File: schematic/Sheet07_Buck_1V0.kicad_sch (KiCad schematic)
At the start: 14 parts, among them U5 TPS7H5001-SP

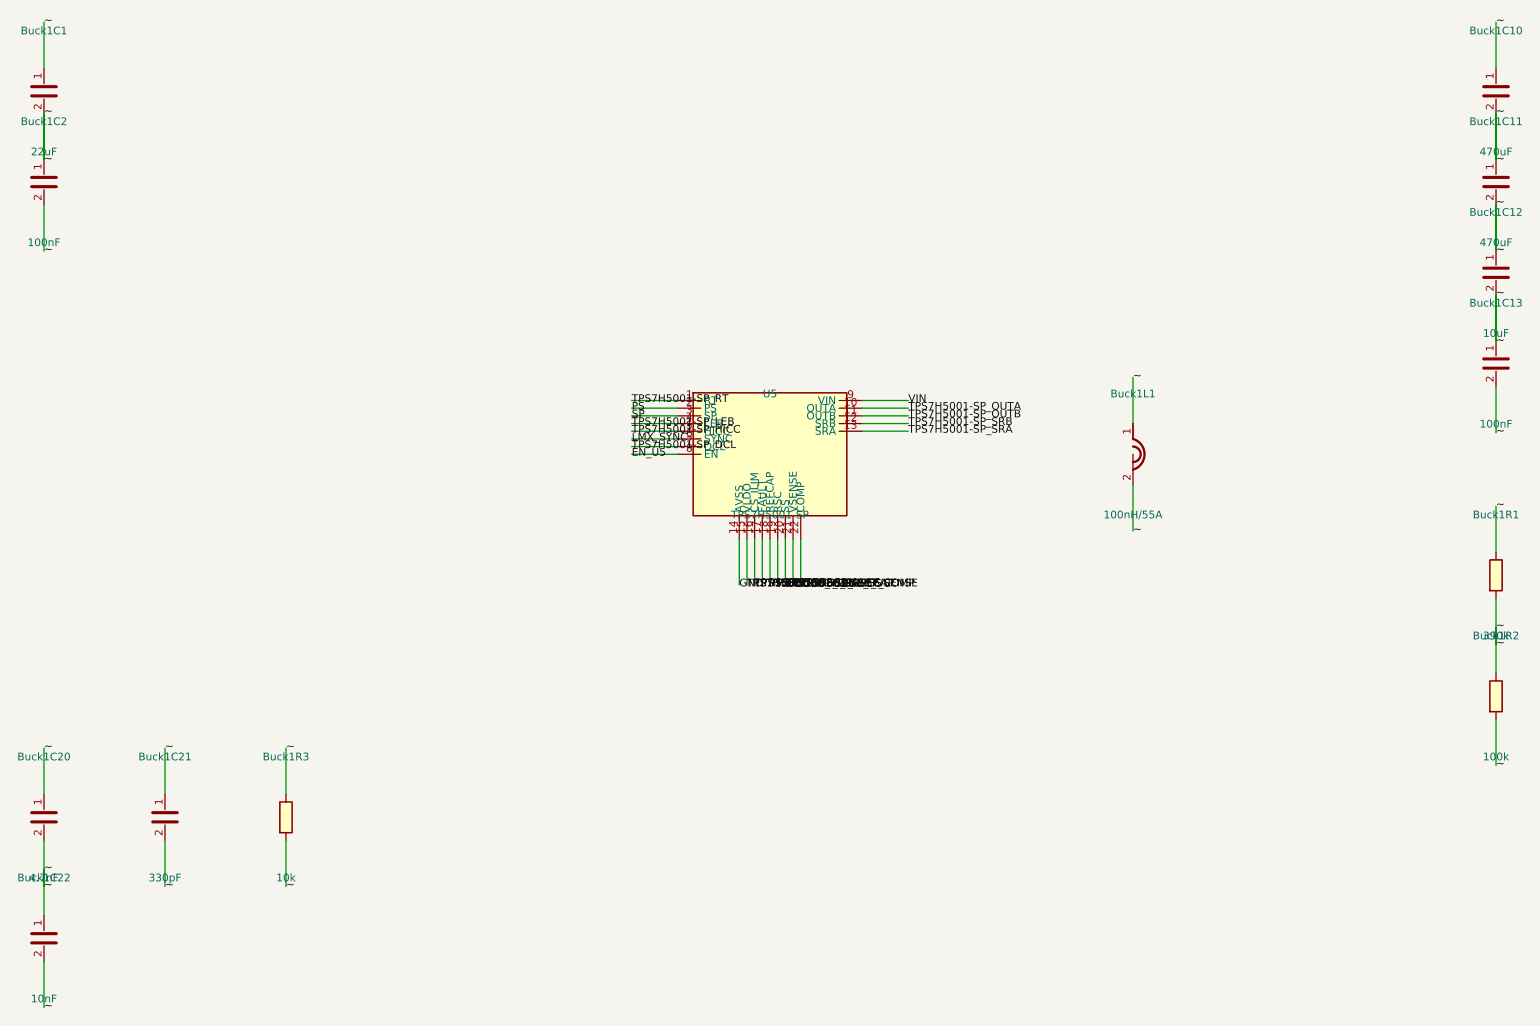
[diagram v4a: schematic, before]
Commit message: fix: use horizontal wire stubs to prevent KiCad net merging
Root cause: vertical wires from stacked power pins (1.27mm spacing)
overlapped when wire length > pin spacing, causing KiCad to merge
all power nets into one. Also skip unnamed (~) passive component pins.

Changes:
- Always use horizontal LEFT stubs regardless of pin angle
- Skip pins with net_name '~' (capacitor/resistor unnamed pins)
- 557 pin connections across 13 sheets, all pass KiCad CLI

NOTE: power net separation still shows all power_in pins on one net
in kicad-cli netlist export - needs further investigation.
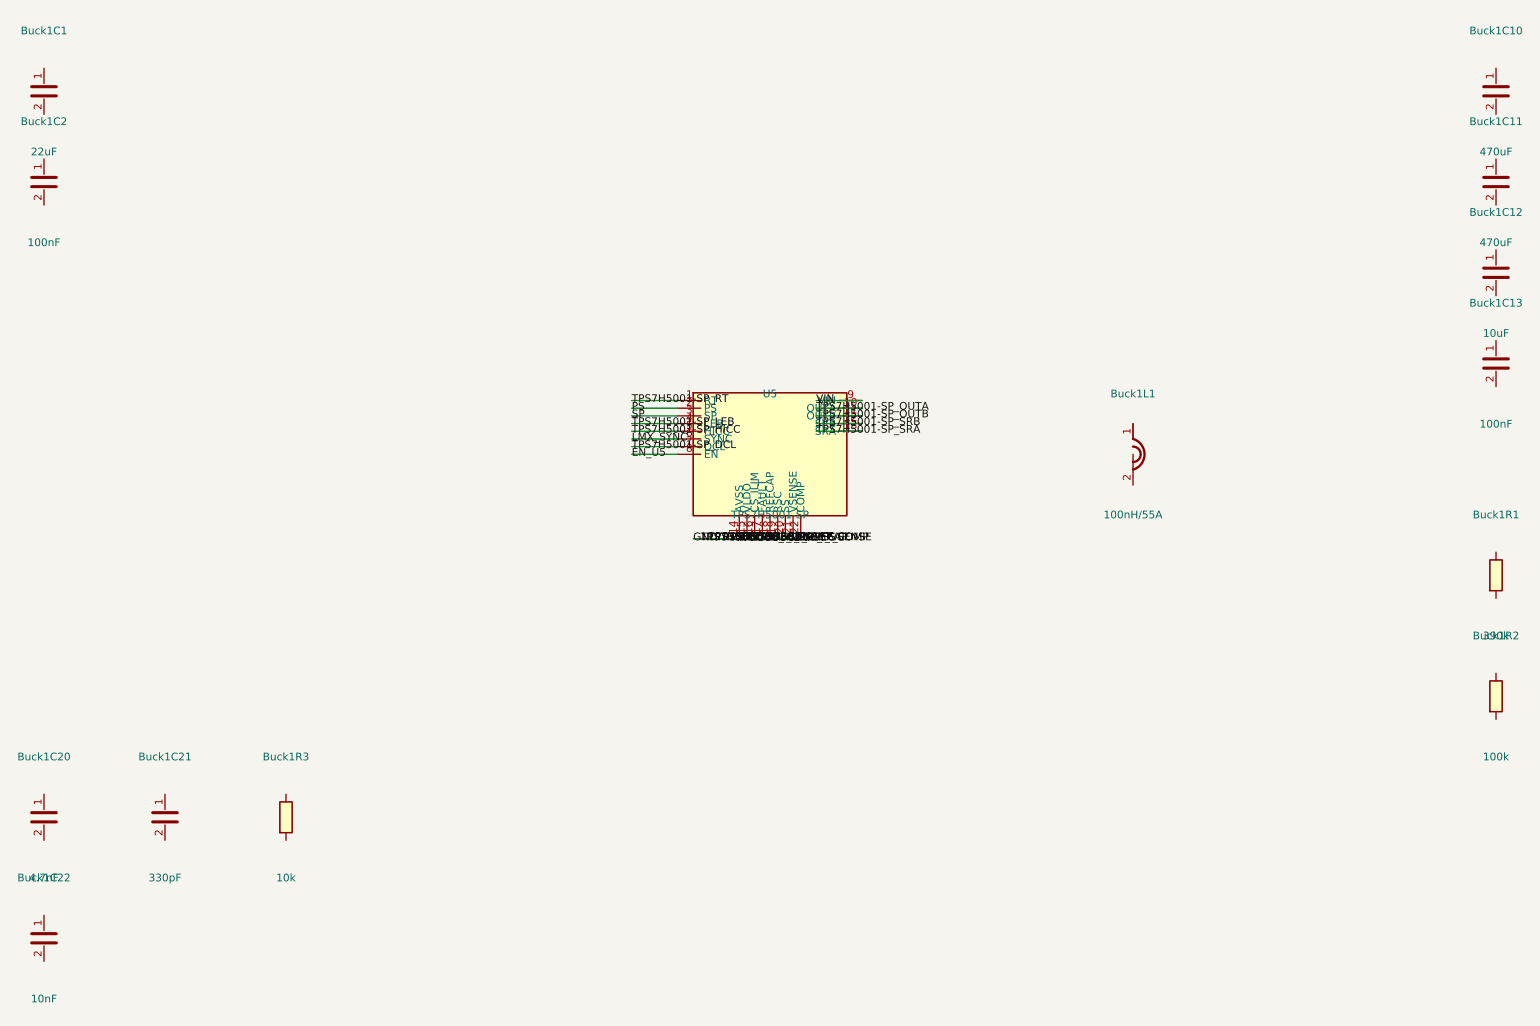
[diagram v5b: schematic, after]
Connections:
- net RSC is gone; now on net GND: U5.19 (RSC)
- net TPS7H5001-SP_COMP is gone; now on net GND: U5.22 (COMP)
- net TPS7H5001-SP_CS is gone; now on net GND: U5.16 (CS_ILIM)
- net TPS7H5001-SP_FAULT is gone; now on net GND: U5.17 (FAULT)
- net TPS7H5001-SP_REFCAP is gone; now on net GND: U5.18 (REFCAP)
- net TPS7H5001-SP_SS is gone; now on net GND: U5.20 (SS)
- net TPS7H5001-SP_VLDO is gone; now on net GND: U5.15 (VLDO)
- net TPS7H5001-SP_VSENSE is gone; now on net GND: U5.21 (VSENSE)
- removed net ~: Buck1C1.1, Buck1C1.2, Buck1C10.1, Buck1C10.2, Buck1C11.1, Buck1C11.2, Buck1C12.1, Buck1C12.2, Buck1C13.1, Buck1C13.2, Buck1C2.1, Buck1C2.2, Buck1C20.1, Buck1C20.2, Buck1C21.1, Buck1C21.2, Buck1C22.1, Buck1C22.2, Buck1L1.1, Buck1L1.2, Buck1R1.1, Buck1R1.2, Buck1R2.1, Buck1R2.2, Buck1R3.1, Buck1R3.2
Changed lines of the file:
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@@
   (wire (pts (xy 184.7600 100.0000) (xy 177.1400 100.0000)) (stroke (width 0) (type default)))
   (label "EN_U5" (at 177.1400 100.0000 0) (effects (font (size 1.27 1.27))))
-  (wire (pts (xy 215.2400 91.1100) (xy 222.8600 91.1100)) (stroke (width 0) (type default)))
-  (label "VIN" (at 222.8600 91.1100 0) (effects (font (size 1.27 1.27))))
-  (wire (pts (xy 215.2400 92.3800) (xy 222.8600 92.3800)) (stroke (width 0) (type default)))
-  (label "TPS7H5001-SP_OUTA" (at 222.8600 92.3800 0) (effects (font (size 1.27 1.27))))
-  (wire (pts (xy 215.2400 93.6500) (xy 222.8600 93.6500)) (stroke (width 0) (type default)))
-  (label "TPS7H5001-SP_OUTB" (at 222.8600 93.6500 0) (effects (font (size 1.27 1.27))))
-  (wire (pts (xy 215.2400 94.9200) (xy 222.8600 94.9200)) (stroke (width 0) (type default)))
-  (label "TPS7H5001-SP_SRB" (at 222.8600 94.9200 0) (effects (font (size 1.27 1.27))))
-  (wire (pts (xy 215.2400 96.1900) (xy 222.8600 96.1900)) (stroke (width 0) (type default)))
-  (label "TPS7H5001-SP_SRA" (at 222.8600 96.1900 0) (effects (font (size 1.27 1.27))))
-  (wire (pts (xy 194.9200 113.9700) (xy 194.9200 121.5900)) (stroke (width 0) (type default)))
-  (label "GND" (at 194.9200 121.5900 0) (effects (font (size 1.27 1.27))))
-  (wire (pts (xy 196.1900 113.9700) (xy 196.1900 121.5900)) (stroke (width 0) (type default)))
-  (label "TPS7H5001-SP_VLDO" (at 196.1900 121.5900 0) (effects (font (size 1.27 1.27))))
-  (wire (pts (xy 197.4600 113.9700) (xy 197.4600 121.5900)) (stroke (width 0) (type default)))
-  (label "TPS7H5001-SP_CS" (at 197.4600 121.5900 0) (effects (font (size 1.27 1.27))))
-  (wire (pts (xy 198.7300 113.9700) (xy 198.7300 121.5900)) (stroke (width 0) (type default)))
-  (label "TPS7H5001-SP_FAULT" (at 198.7300 121.5900 0) (effects (font (size 1.27 1.27))))
-  (wire (pts (xy 200.0000 113.9700) (xy 200.0000 121.5900)) (stroke (width 0) (type default)))
-  (label "TPS7H5001-SP_REFCAP" (at 200.0000 121.5900 0) (effects (font (size 1.27 1.27))))
-  (wire (pts (xy 201.2700 113.9700) (xy 201.2700 121.5900)) (stroke (width 0) (type default)))
-  (label "RSC" (at 201.2700 121.5900 0) (effects (font (size 1.27 1.27))))
-  (wire (pts (xy 202.5400 113.9700) (xy 202.5400 121.5900)) (stroke (width 0) (type default)))
-  (label "TPS7H5001-SP_SS" (at 202.5400 121.5900 0) (effects (font (size 1.27 1.27))))
-  (wire (pts (xy 203.8100 113.9700) (xy 203.8100 121.5900)) (stroke (width 0) (type default)))
-  (label "TPS7H5001-SP_VSENSE" (at 203.8100 121.5900 0) (effects (font (size 1.27 1.27))))
-  (wire (pts (xy 205.0800 113.9700) (xy 205.0800 121.5900)) (stroke (width 0) (type default)))
-  (label "TPS7H5001-SP_COMP" (at 205.0800 121.5900 0) (effects (font (size 1.27 1.27))))
-  (wire (pts (xy 80.0000 36.1900) (xy 80.0000 28.5700)) (stroke (width 0) (type default)))
-  (label "~" (at 80.0000 28.5700 0) (effects (font (size 1.27 1.27))))
-  (wire (pts (xy 80.0000 43.8100) (xy 80.0000 51.4300)) (stroke (width 0) (type default)))
-  (label "~" (at 80.0000 51.4300 0) (effects (font (size 1.27 1.27))))
-  (wire (pts (xy 80.0000 51.1900) (xy 80.0000 43.5700)) (stroke (width 0) (type default)))
-  (label "~" (at 80.0000 43.5700 0) (effects (font (size 1.27 1.27))))
-  (wire (pts (xy 80.0000 58.8100) (xy 80.0000 66.4300)) (stroke (width 0) (type default)))
-  (label "~" (at 80.0000 66.4300 0) (effects (font (size 1.27 1.27))))
-  (wire (pts (xy 320.0000 36.1900) (xy 320.0000 28.5700)) (stroke (width 0) (type default)))
-  (label "~" (at 320.0000 28.5700 0) (effects (font (size 1.27 1.27))))
-  (wire (pts (xy 320.0000 43.8100) (xy 320.0000 51.4300)) (stroke (width 0) (type default)))
-  (label "~" (at 320.0000 51.4300 0) (effects (font (size 1.27 1.27))))
-  (wire (pts (xy 320.0000 51.1900) (xy 320.0000 43.5700)) (stroke (width 0) (type default)))
-  (label "~" (at 320.0000 43.5700 0) (effects (font (size 1.27 1.27))))
-  (wire (pts (xy 320.0000 58.8100) (xy 320.0000 66.4300)) (stroke (width 0) (type default)))
-  (label "~" (at 320.0000 66.4300 0) (effects (font (size 1.27 1.27))))
-  (wire (pts (xy 320.0000 66.1900) (xy 320.0000 58.5700)) (stroke (width 0) (type default)))
-  (label "~" (at 320.0000 58.5700 0) (effects (font (size 1.27 1.27))))
-  (wire (pts (xy 320.0000 73.8100) (xy 320.0000 81.4300)) (stroke (width 0) (type default)))
-  (label "~" (at 320.0000 81.4300 0) (effects (font (size 1.27 1.27))))
-  (wire (pts (xy 320.0000 81.1900) (xy 320.0000 73.5700)) (stroke (width 0) (type default)))
-  (label "~" (at 320.0000 73.5700 0) (effects (font (size 1.27 1.27))))
-  (wire (pts (xy 320.0000 88.8100) (xy 320.0000 96.4300)) (stroke (width 0) (type default)))
-  (label "~" (at 320.0000 96.4300 0) (effects (font (size 1.27 1.27))))
-  (wire (pts (xy 260.0000 94.9200) (xy 260.0000 87.3000)) (stroke (width 0) (type default)))
-  (label "~" (at 260.0000 87.3000 0) (effects (font (size 1.27 1.27))))
-  (wire (pts (xy 260.0000 105.0800) (xy 260.0000 112.7000)) (stroke (width 0) (type default)))
-  (label "~" (at 260.0000 112.7000 0) (effects (font (size 1.27 1.27))))
-  (wire (pts (xy 320.0000 116.1900) (xy 320.0000 108.5700)) (stroke (width 0) (type default)))
-  (label "~" (at 320.0000 108.5700 0) (effects (font (size 1.27 1.27))))
-  (wire (pts (xy 320.0000 123.8100) (xy 320.0000 131.4300)) (stroke (width 0) (type default)))
-  (label "~" (at 320.0000 131.4300 0) (effects (font (size 1.27 1.27))))
-  (wire (pts (xy 320.0000 136.1900) (xy 320.0000 128.5700)) (stroke (width 0) (type default)))
-  (label "~" (at 320.0000 128.5700 0) (effects (font (size 1.27 1.27))))
-  (wire (pts (xy 320.0000 143.8100) (xy 320.0000 151.4300)) (stroke (width 0) (type default)))
-  (label "~" (at 320.0000 151.4300 0) (effects (font (size 1.27 1.27))))
-  (wire (pts (xy 80.0000 156.1900) (xy 80.0000 148.5700)) (stroke (width 0) (type default)))
-  (label "~" (at 80.0000 148.5700 0) (effects (font (size 1.27 1.27))))
-  (wire (pts (xy 80.0000 163.8100) (xy 80.0000 171.4300)) (stroke (width 0) (type default)))
-  (label "~" (at 80.0000 171.4300 0) (effects (font (size 1.27 1.27))))
-  (wire (pts (xy 100.0000 156.1900) (xy 100.0000 148.5700)) (stroke (width 0) (type default)))
-  (label "~" (at 100.0000 148.5700 0) (effects (font (size 1.27 1.27))))
-  (wire (pts (xy 100.0000 163.8100) (xy 100.0000 171.4300)) (stroke (width 0) (type default)))
-  (label "~" (at 100.0000 171.4300 0) (effects (font (size 1.27 1.27))))
-  (wire (pts (xy 120.0000 156.1900) (xy 120.0000 148.5700)) (stroke (width 0) (type default)))
-  (label "~" (at 120.0000 148.5700 0) (effects (font (size 1.27 1.27))))
-  (wire (pts (xy 120.0000 163.8100) (xy 120.0000 171.4300)) (stroke (width 0) (type default)))
-  (label "~" (at 120.0000 171.4300 0) (effects (font (size 1.27 1.27))))
-  (wire (pts (xy 80.0000 176.1900) (xy 80.0000 168.5700)) (stroke (width 0) (type default)))
-  (label "~" (at 80.0000 168.5700 0) (effects (font (size 1.27 1.27))))
-  (wire (pts (xy 80.0000 183.8100) (xy 80.0000 191.4300)) (stroke (width 0) (type default)))
-  (label "~" (at 80.0000 191.4300 0) (effects (font (size 1.27 1.27))))
+  (wire (pts (xy 215.2400 91.1100) (xy 207.6200 91.1100)) (stroke (width 0) (type default)))
+  (label "VIN" (at 207.6200 91.1100 0) (effects (font (size 1.27 1.27))))
+  (wire (pts (xy 215.2400 92.3800) (xy 207.6200 92.3800)) (stroke (width 0) (type default)))
+  (label "TPS7H5001-SP_OUTA" (at 207.6200 92.3800 0) (effects (font (size 1.27 1.27))))
+  (wire (pts (xy 215.2400 93.6500) (xy 207.6200 93.6500)) (stroke (width 0) (type default)))
+  (label "TPS7H5001-SP_OUTB" (at 207.6200 93.6500 0) (effects (font (size 1.27 1.27))))
+  (wire (pts (xy 215.2400 94.9200) (xy 207.6200 94.9200)) (stroke (width 0) (type default)))
+  (label "TPS7H5001-SP_SRB" (at 207.6200 94.9200 0) (effects (font (size 1.27 1.27))))
+  (wire (pts (xy 215.2400 96.1900) (xy 207.6200 96.1900)) (stroke (width 0) (type default)))
+  (label "TPS7H5001-SP_SRA" (at 207.6200 96.1900 0) (effects (font (size 1.27 1.27))))
+  (wire (pts (xy 194.9200 113.9700) (xy 187.3000 113.9700)) (stroke (width 0) (type default)))
+  (label "GND" (at 187.3000 113.9700 0) (effects (font (size 1.27 1.27))))
+  (wire (pts (xy 196.1900 113.9700) (xy 188.5700 113.9700)) (stroke (width 0) (type default)))
+  (label "TPS7H5001-SP_VLDO" (at 188.5700 113.9700 0) (effects (font (size 1.27 1.27))))
+  (wire (pts (xy 197.4600 113.9700) (xy 189.8400 113.9700)) (stroke (width 0) (type default)))
+  (label "TPS7H5001-SP_CS" (at 189.8400 113.9700 0) (effects (font (size 1.27 1.27))))
+  (wire (pts (xy 198.7300 113.9700) (xy 191.1100 113.9700)) (stroke (width 0) (type default)))
+  (label "TPS7H5001-SP_FAULT" (at 191.1100 113.9700 0) (effects (font (size 1.27 1.27))))
+  (wire (pts (xy 200.0000 113.9700) (xy 192.3800 113.9700)) (stroke (width 0) (type default)))
+  (label "TPS7H5001-SP_REFCAP" (at 192.3800 113.9700 0) (effects (font (size 1.27 1.27))))
+  (wire (pts (xy 201.2700 113.9700) (xy 193.6500 113.9700)) (stroke (width 0) (type default)))
+  (label "RSC" (at 193.6500 113.9700 0) (effects (font (size 1.27 1.27))))
+  (wire (pts (xy 202.5400 113.9700) (xy 194.9200 113.9700)) (stroke (width 0) (type default)))
+  (label "TPS7H5001-SP_SS" (at 194.9200 113.9700 0) (effects (font (size 1.27 1.27))))
+  (wire (pts (xy 203.8100 113.9700) (xy 196.1900 113.9700)) (stroke (width 0) (type default)))
+  (label "TPS7H5001-SP_VSENSE" (at 196.1900 113.9700 0) (effects (font (size 1.27 1.27))))
+  (wire (pts (xy 205.0800 113.9700) (xy 197.4600 113.9700)) (stroke (width 0) (type default)))
+  (label "TPS7H5001-SP_COMP" (at 197.4600 113.9700 0) (effects (font (size 1.27 1.27))))
   (sheet_instances (path "/" (page "1")))
 )
